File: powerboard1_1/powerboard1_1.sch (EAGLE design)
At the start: 97 parts, among them Q1 IPP80P03P4L04AKSA1, U1 UWQ-12/20-T48NBS-C, U2 UWE-5/20-Q48NB-C, U3 UWE-3.3/30-Q48NB-C

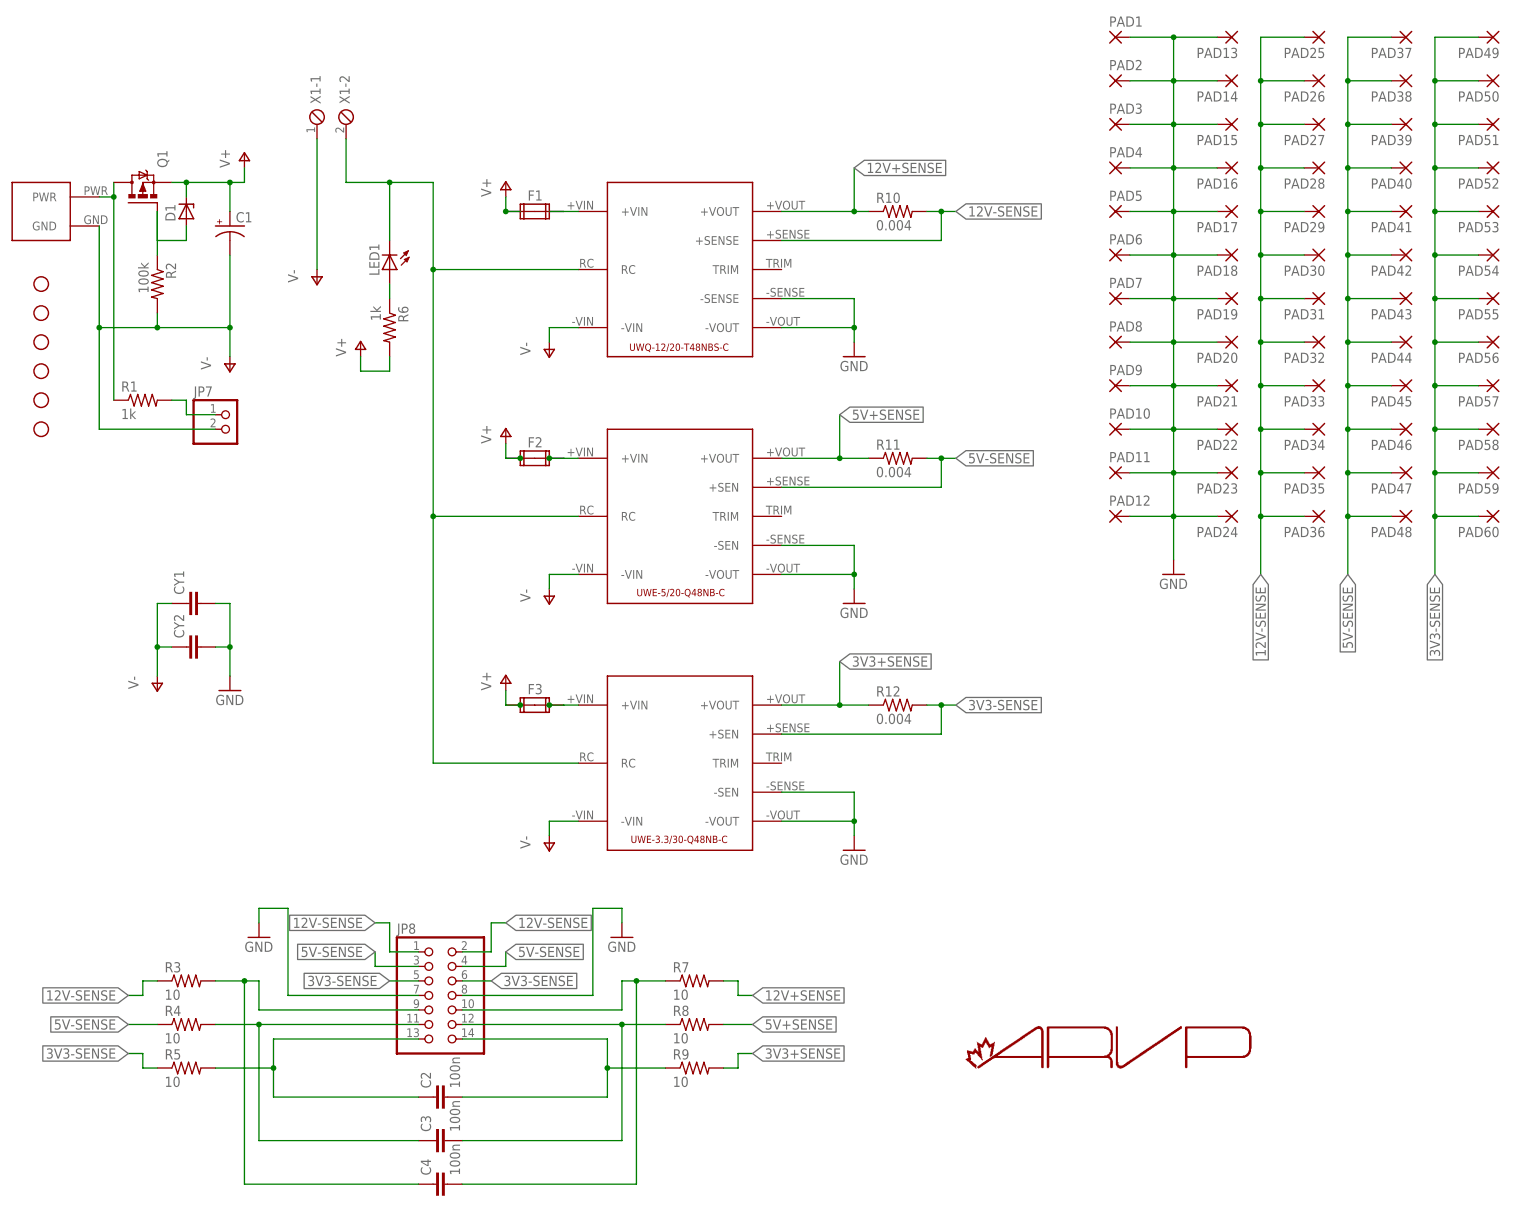
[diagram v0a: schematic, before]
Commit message: Added 4.7k ohm load between V+ and V-; Added fuse between battery terminal and Q1 drain terminal; Added 3 position terminal blocks on each output rail
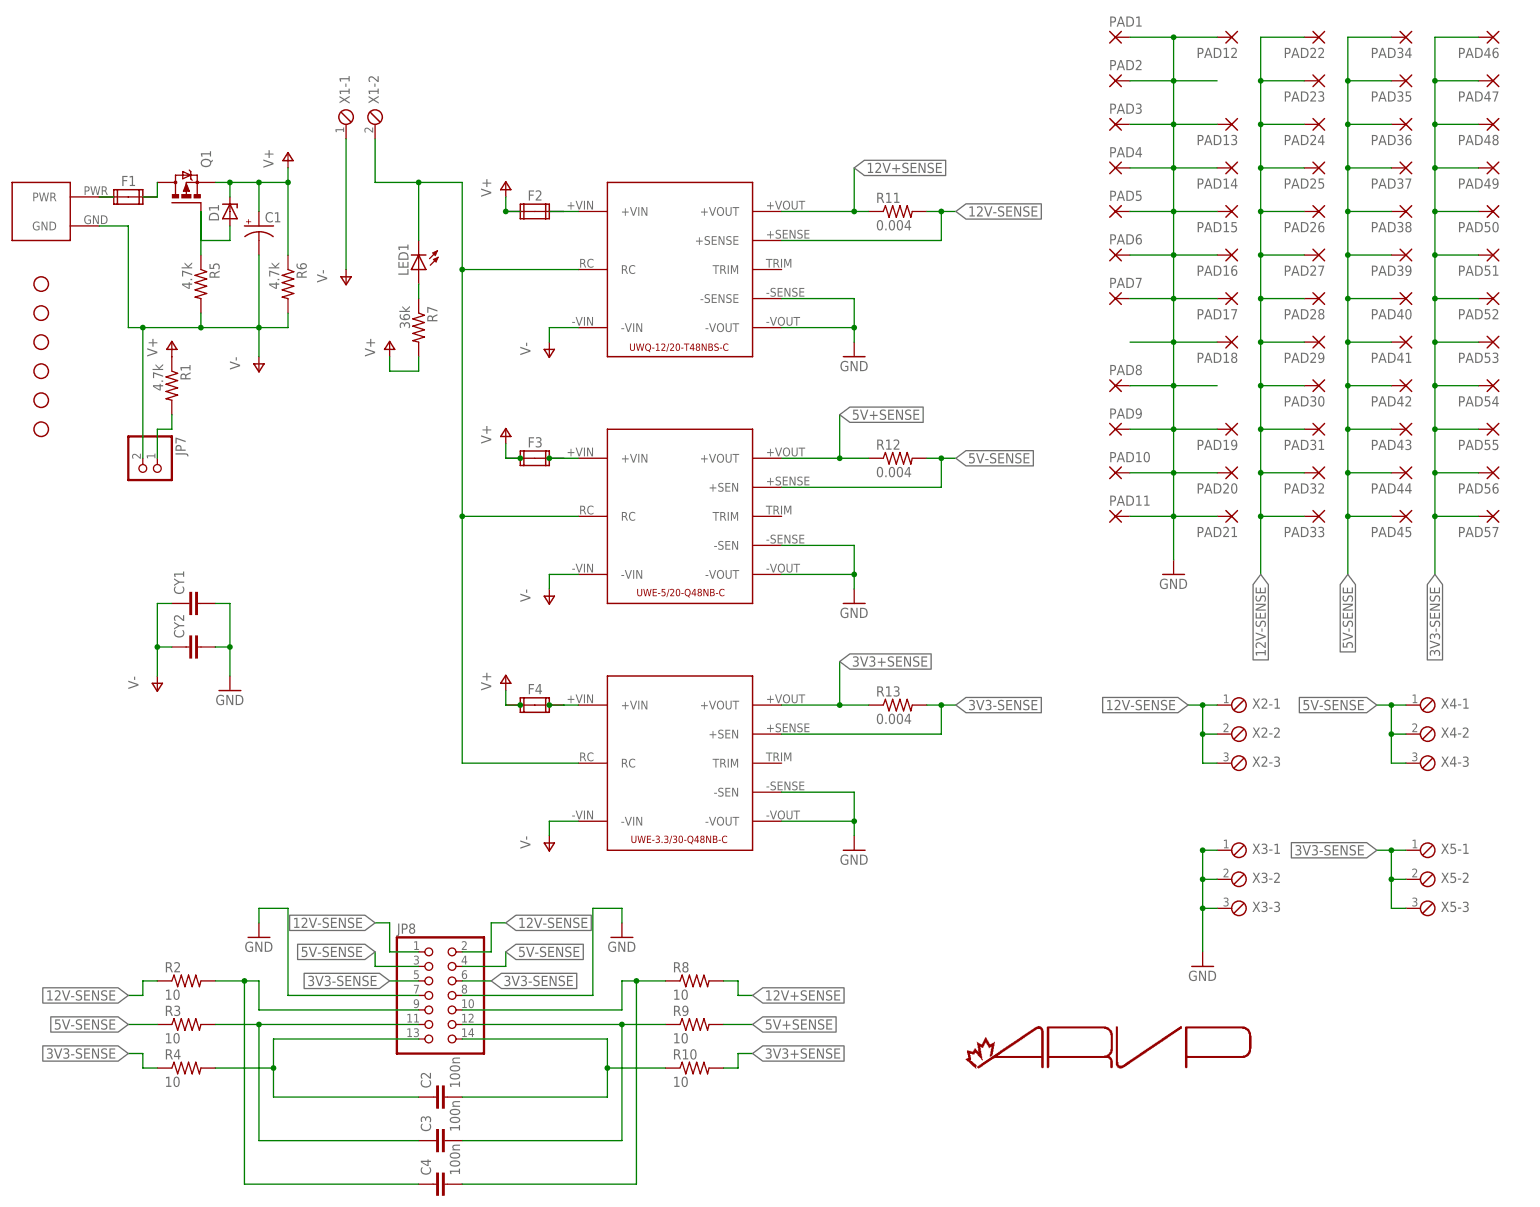
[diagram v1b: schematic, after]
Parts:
- removed PAD58, PAD59, PAD60: WIREPAD3,17/1,3, wirepad:WIREPAD3,17/1,3
- added F4: (no value), special:FUSE2P
- added R13: 0.004, rcl:R-US_0617/22
- added X2, X3, X4, X5: (no value), con-phoenix-254:MPT3
- C1: device rcl:CPOL-USE5-10.5 -> rcl:CPOL-USE2.5-7
- D1: value (none) -> BZV10; device diode:ZENER-DIODEDO35Z10 -> diode:BZV10
- R1, R6: value 1k -> 4.7k
- R10: value 0.004 -> 10; device rcl:R-US_0617/22 -> rcl:R-US_0204/5
- R2: value 100k -> 10; device resistor:R-US_0204/7 -> rcl:R-US_0204/5
- R5: value 10 -> 4.7k; device rcl:R-US_0204/5 -> resistor:R-US_0204/7
- R7: value 10 -> 36k; device rcl:R-US_0204/5 -> resistor:R-US_0204/7
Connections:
- new net N$3: F1.1A, F1.1B, P$1.PWR
- net 12V+SENSE: now also R11.1, R8.2; no longer R10.1, R7.2
- net 12V-SENSE: now also PAD22.P, PAD23.P, PAD24.P, R11.2, R2.1, X2-1.1, X2-2.1, X2-3.1; no longer PAD34.P, PAD35.P, PAD36.P, R10.2, R3.1
- net 3V3+SENSE: now also R10.2, R13.1; no longer R12.1, R9.2
- net 3V3-SENSE: now also PAD46.P, PAD47.P, PAD48.P, R13.2, R4.1, X5-1.1, X5-2.1, X5-3.1; no longer PAD58.P, PAD59.P, PAD60.P, R12.2, R5.1
- net 5V+SENSE: now also R12.1, R9.2; no longer R11.1, R8.2
- net 5V-SENSE: now also PAD34.P, PAD35.P, PAD36.P, R12.2, R3.1, X4-1.1, X4-2.1, X4-3.1; no longer PAD46.P, PAD47.P, PAD48.P, R11.2, R4.1
- net GND: now also X3-1.1, X3-2.1, X3-3.1; no longer PAD22.P, PAD23.P, PAD24.P
- net J3: now also R2.2; no longer R3.2
- net J4: now also R8.1; no longer R7.1
- net J5: now also R3.2; no longer R4.2
- net J6: now also R9.1; no longer R8.1
- net J7: now also R4.2; no longer R5.2
- net J8: now also R10.1; no longer R9.1
- net N$1: now also R7.1; no longer R6.1
- net N$4: now also R5.1; no longer R2.1
- net N$5: now also F2.2A, F2.2B; no longer F1.2A, F1.2B
- net N$6: now also F3.2A, F3.2B; no longer F2.2A, F2.2B
- net N$7: now also F4.2A, F4.2B; no longer F3.2A, F3.2B
- net V+: now also F4.1A, F4.1B, R1.1, R6.1, R7.2; no longer F1.1A, F1.1B, R6.2
- net V-: now also R5.2, R6.2; no longer R2.2
- net VBAT+: now also F1.2A, F1.2B; no longer P$1.PWR, R1.1
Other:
- moved on the sheet: C1, F1, F2, F3, JP7, LED1, PAD10, PAD11, PAD12, PAD13, PAD14, PAD15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

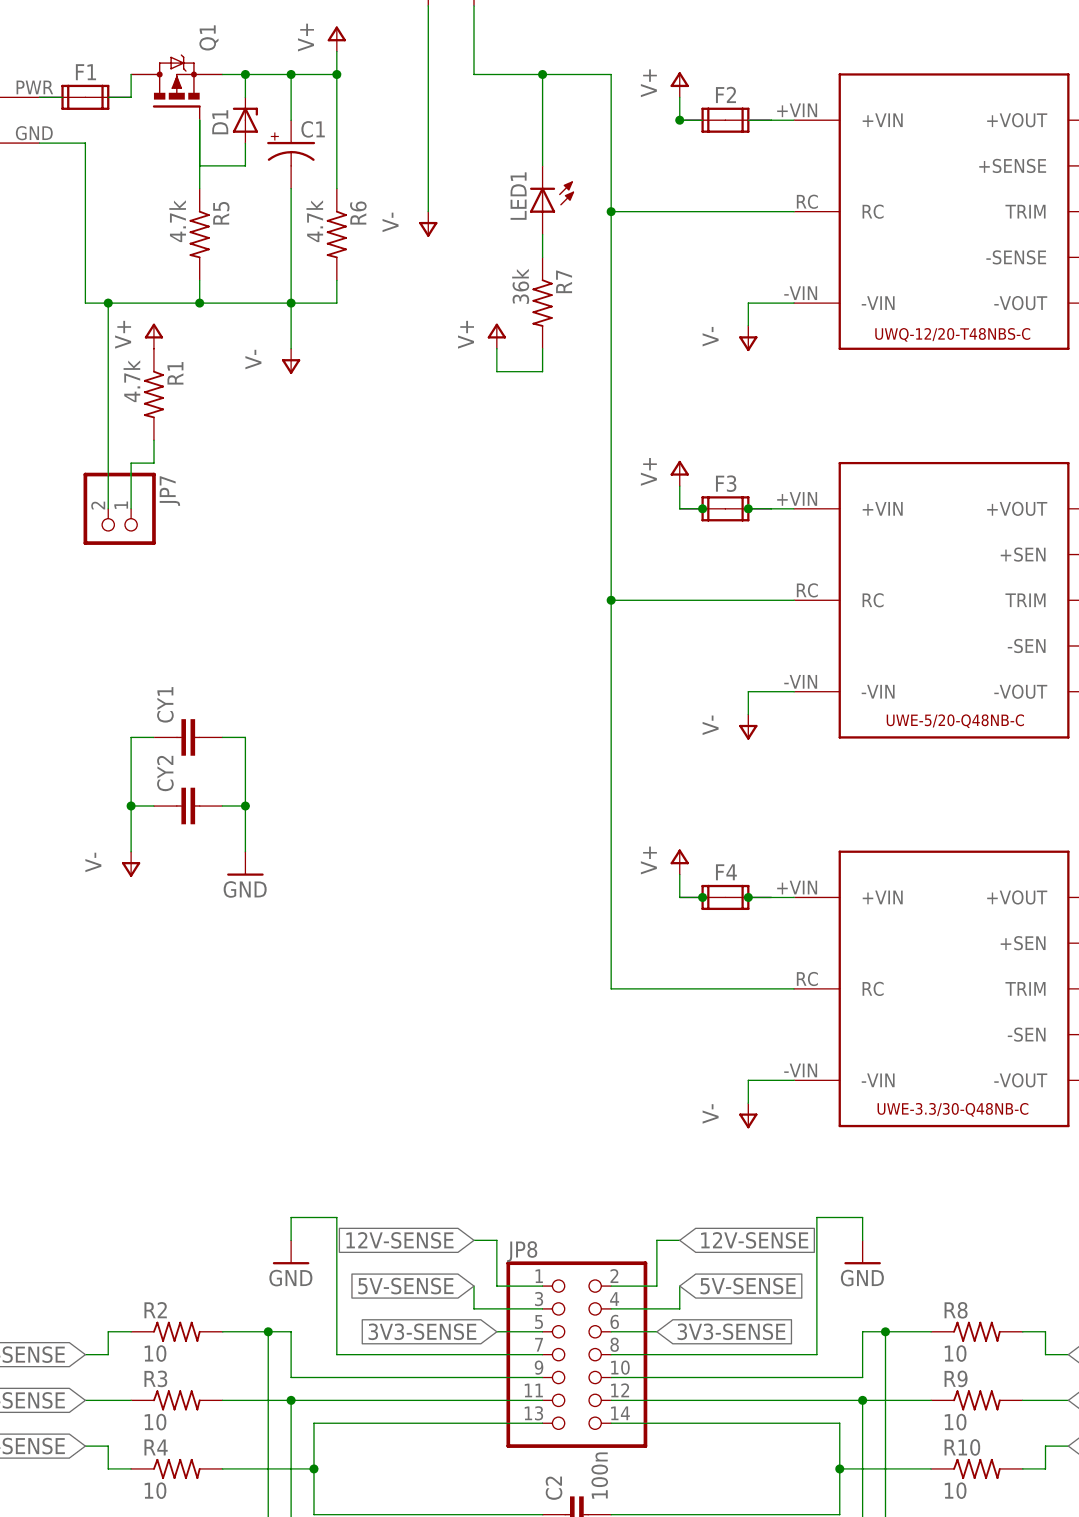
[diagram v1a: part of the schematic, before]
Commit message: Changed value of R5 to 2k; Changed footprint of C1; Modified polygons and traces
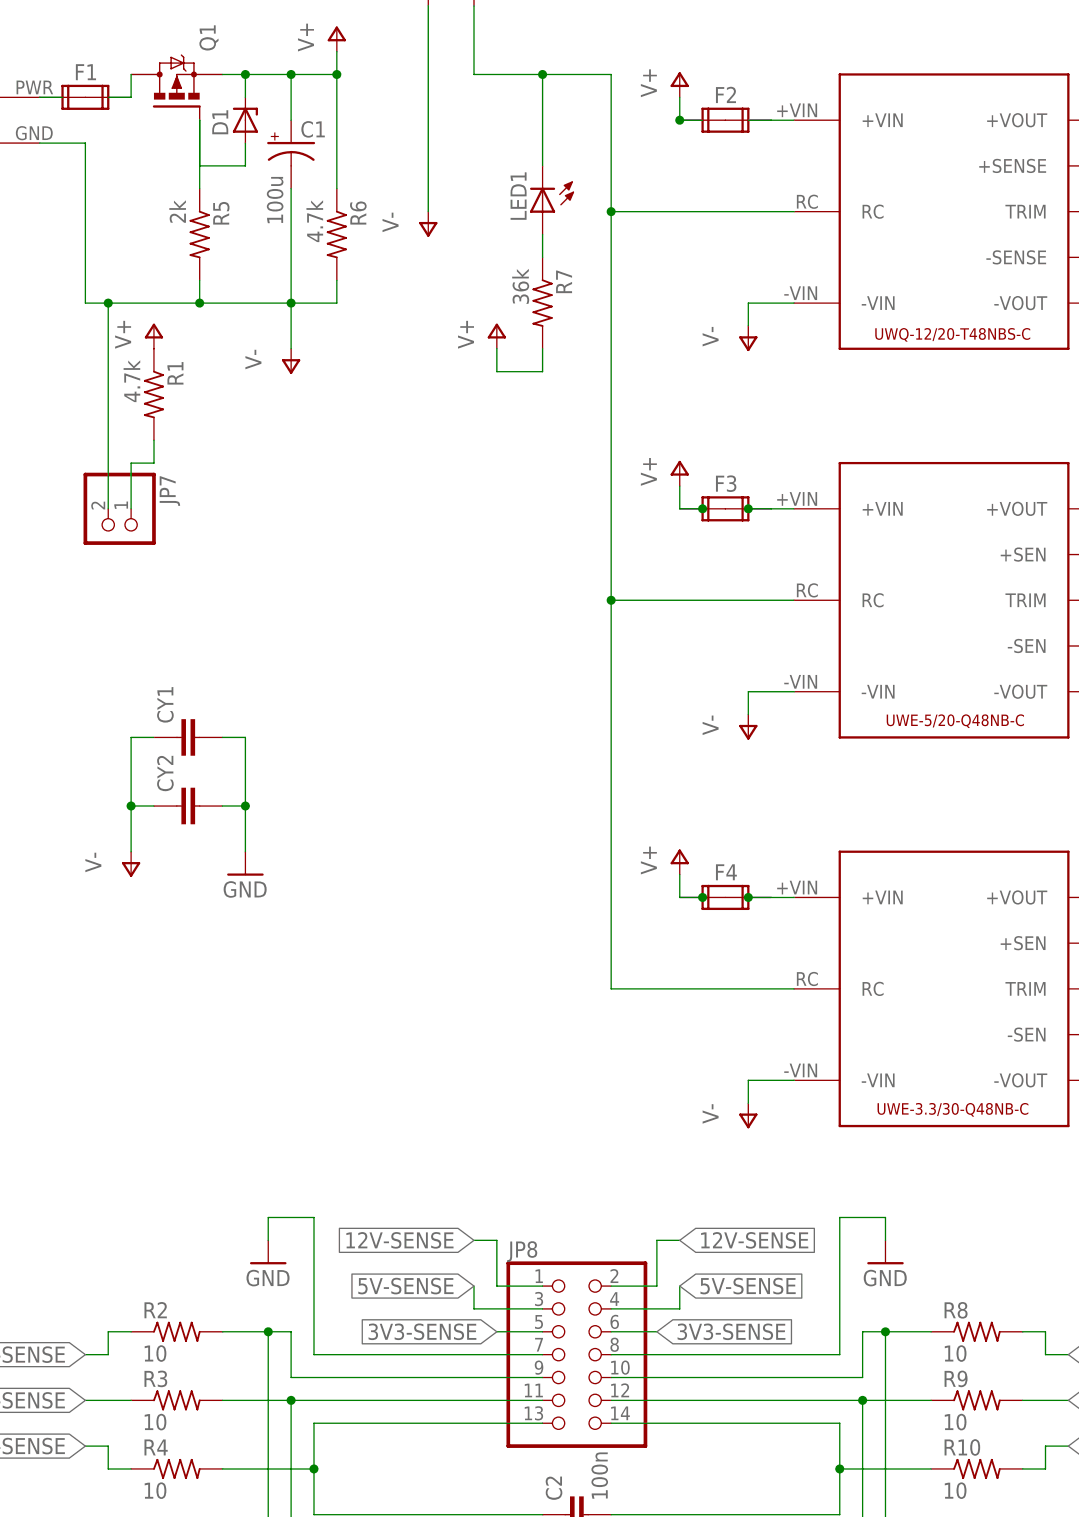
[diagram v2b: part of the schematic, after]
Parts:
- C1: value (none) -> 100u; device rcl:CPOL-USE2.5-7 -> rcl:CPOL-USE3.5-8
- R5: value 4.7k -> 2k
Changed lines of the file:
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@@
 <part name="GND7" library="supply1" deviceset="GND" device=""/>
 <part name="Q1" library="transistor-power" deviceset="IPP80P03P4L04AKSA1" device=""/>
-<part name="R5" library="resistor" deviceset="R-US_" device="0204/7" value="4.7k"/>
+<part name="R5" library="resistor" deviceset="R-US_" device="0204/7" value="2k"/>
 <part name="P+3" library="supply1" deviceset="V+" device=""/>
 <part name="JP7" library="pinhead" deviceset="PINHD-1X2" device=""/>
@@
 <part name="F1" library="special" deviceset="FUSE2P" device=""/>
 <part name="D1" library="diode" deviceset="BZV10" device=""/>
-<part name="C1" library="rcl" deviceset="CPOL-US" device="E2.5-7"/>
+<part name="C1" library="rcl" deviceset="CPOL-US" device="E3.5-8" value="100u"/>
 </parts>
 <sheets>
@@
 <instance part="X1" gate="-2" x="76.2" y="243.84" rot="R90"/>
 <instance part="JP8" gate="A" x="86.36" y="91.44"/>
-<instance part="GND3" gate="1" x="119.38" y="101.6"/>
-<instance part="GND2" gate="1" x="55.88" y="101.6"/>
+<instance part="GND3" gate="1" x="121.92" y="101.6"/>
+<instance part="GND2" gate="1" x="53.34" y="101.6"/>
 <instance part="R6" gate="G$1" x="60.96" y="215.9" rot="R270"/>
 <instance part="GND8" gate="1" x="220.98" y="96.52"/>
@@
 <attribute name="NAME" x="48.895" y="226.822" size="1.778" layer="95" rot="R90"/>
 </instance>
-<instance part="C1" gate="G$1" x="55.88" y="226.06"/>
+<instance part="C1" gate="G$1" x="55.88" y="226.06" smashed="yes">
+<attribute name="NAME" x="56.896" y="226.695" size="1.778" layer="95"/>
+<attribute name="VALUE" x="54.991" y="216.916" size="1.778" layer="96" rot="R90"/>
+</instance>
 </instances>
 <busses>
@@
 <segment>
 <pinref part="JP8" gate="A" pin="8"/>
-<wire x1="91.44" y1="91.44" x2="114.3" y2="91.44" width="0.1524" layer="91"/>
-<wire x1="114.3" y1="91.44" x2="114.3" y2="106.68" width="0.1524" layer="91"/>
-<wire x1="114.3" y1="106.68" x2="119.38" y2="106.68" width="0.1524" layer="91"/>
-<wire x1="119.38" y1="106.68" x2="119.38" y2="104.14" width="0.1524" layer="91"/>
+<wire x1="91.44" y1="91.44" x2="116.84" y2="91.44" width="0.1524" layer="91"/>
+<wire x1="116.84" y1="91.44" x2="116.84" y2="106.68" width="0.1524" layer="91"/>
+<wire x1="116.84" y1="106.68" x2="121.92" y2="106.68" width="0.1524" layer="91"/>
+<wire x1="121.92" y1="106.68" x2="121.92" y2="104.14" width="0.1524" layer="91"/>
 <pinref part="GND3" gate="1" pin="GND"/>
 </segment>
 <segment>
 <pinref part="JP8" gate="A" pin="7"/>
-<wire x1="83.82" y1="91.44" x2="60.96" y2="91.44" width="0.1524" layer="91"/>
-<wire x1="60.96" y1="91.44" x2="60.96" y2="106.68" width="0.1524" layer="91"/>
-<wire x1="60.96" y1="106.68" x2="55.88" y2="106.68" width="0.1524" layer="91"/>
-<wire x1="55.88" y1="106.68" x2="55.88" y2="104.14" width="0.1524" layer="91"/>
+<wire x1="83.82" y1="91.44" x2="58.42" y2="91.44" width="0.1524" layer="91"/>
+<wire x1="58.42" y1="91.44" x2="58.42" y2="106.68" width="0.1524" layer="91"/>
+<wire x1="58.42" y1="106.68" x2="53.34" y2="106.68" width="0.1524" layer="91"/>
+<wire x1="53.34" y1="106.68" x2="53.34" y2="104.14" width="0.1524" layer="91"/>
 <pinref part="GND2" gate="1" pin="GND"/>
 </segment>
